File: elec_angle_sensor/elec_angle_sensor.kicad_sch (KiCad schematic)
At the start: 13 parts, among them J7 JST SH, U1 AS5600L

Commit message: [update] Full schematic + positionning
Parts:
- added H4: Mounting Holes M2,5, MountingHole:MountingHole_2.7mm_M2.5_ISO7380_Pad_TopBottom, symbol Mechanical:MountingHole_Pad
- added H5: MountingHole_Pad, MountingHole:MountingHole_2.7mm_M2.5_ISO7380_Pad_TopBottom, symbol Mechanical:MountingHole_Pad
- added H6, H7: Centering Hole 2 mm, Library_Pollen:MountingHole_2.0mm, symbol Mechanical:MountingHole
- added J1: JST SH, Connector_JST:JST_SH_SM04B-SRSS-TB_1x04-1MP_P1.00mm_Horizontal, symbol Connector_Generic_MountingPin:Conn_01x04_MountingPin
- G1: footprint Sparkfun-Qwiic:qwiic_5mm -> Library_Pollen:Logo_qwiic_5mm; symbol Sparkfun-Qwiic:qwiic_Logo -> Library_Pollen:Logo qwiic; now in the parts list
- J7: footprint Connector_JST:JST_SH_BM04B-SRSS-TB_1x04-1MP_P1.00mm_Vertical -> Connector_JST:JST_SH_SM04B-SRSS-TB_1x04-1MP_P1.00mm_Horizontal; LCSC Part C160390 -> C160404
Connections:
- net +3V3: now also J1.2 (Pin_2)
- net GND: now also H4.1, H5.1, J1.1 (Pin_1), J1.MP (MountPin)
- net at D1.3 (K), J7.3 (Pin_3), R1.2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: now also J1.3 (Pin_3)
- net at D1.4 (K), J7.4 (Pin_4), R2.2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: now also J1.4 (Pin_4)
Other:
- moved on the sheet: J7

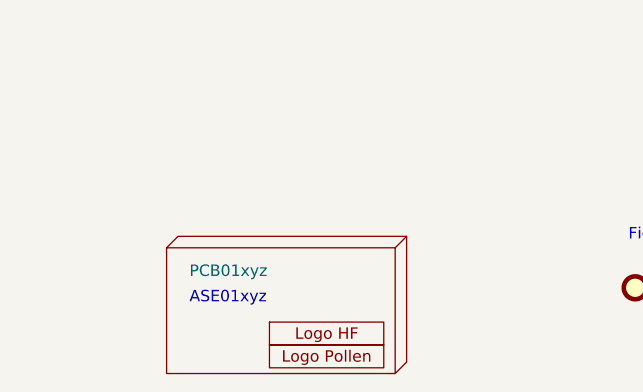
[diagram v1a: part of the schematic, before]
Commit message: [update] Angle+IMU are routed ERC OK
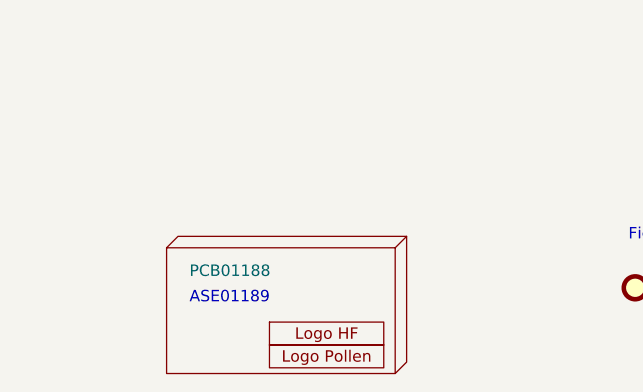
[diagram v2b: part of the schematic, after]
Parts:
- H1: value PCB01xyz -> PCB01188
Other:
- note added: "ASE01189"
- note removed: "ASE01xyz"
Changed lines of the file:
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@@
 		)
 	)
-	(text "ASE01xyz"
+	(text "ASE01189"
 		(exclude_from_sim no)
 		(at 38.1 172.085 0)
@@
 			)
 		)
-		(property "Value" "PCB01xyz"
+		(property "Value" "PCB01188"
 			(at 38.1 168.275 0)
 			(effects

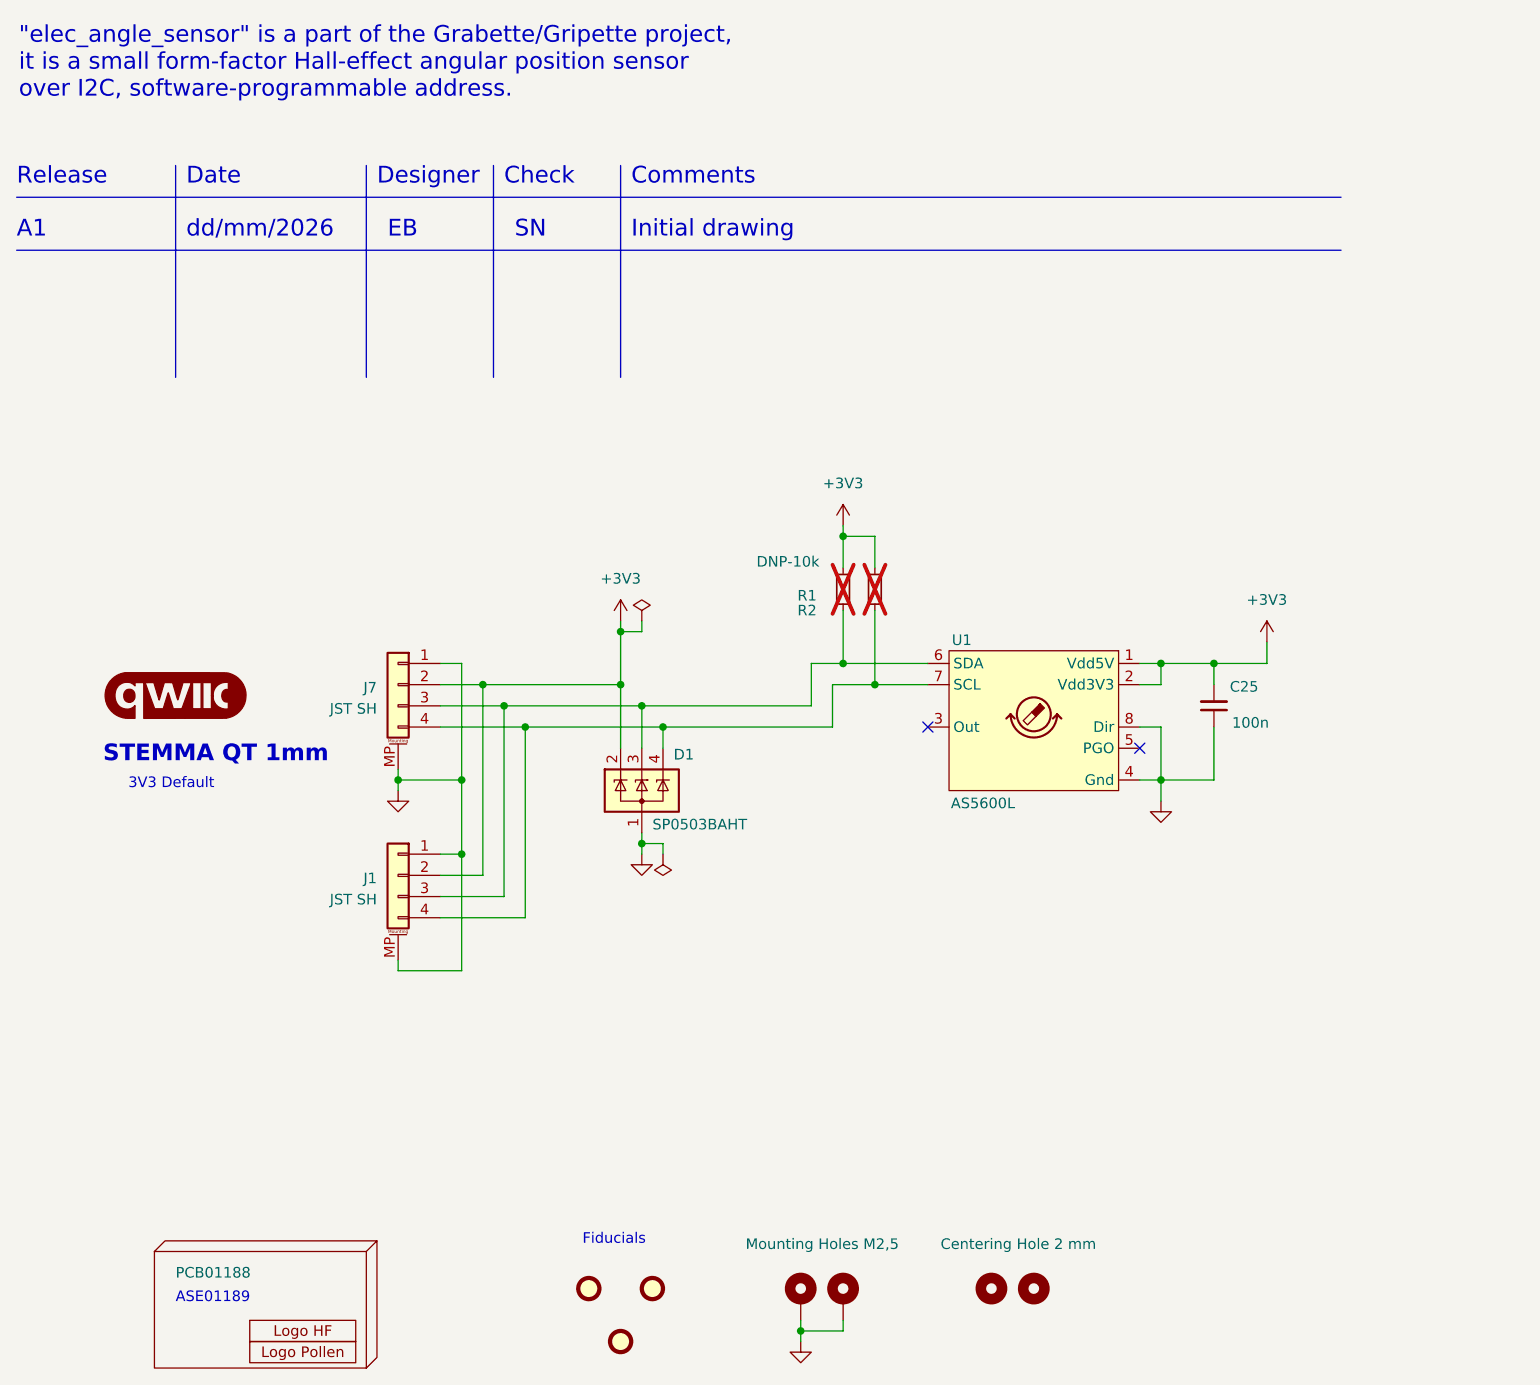
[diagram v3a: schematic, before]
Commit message: [added] Gripette-specific DCDC
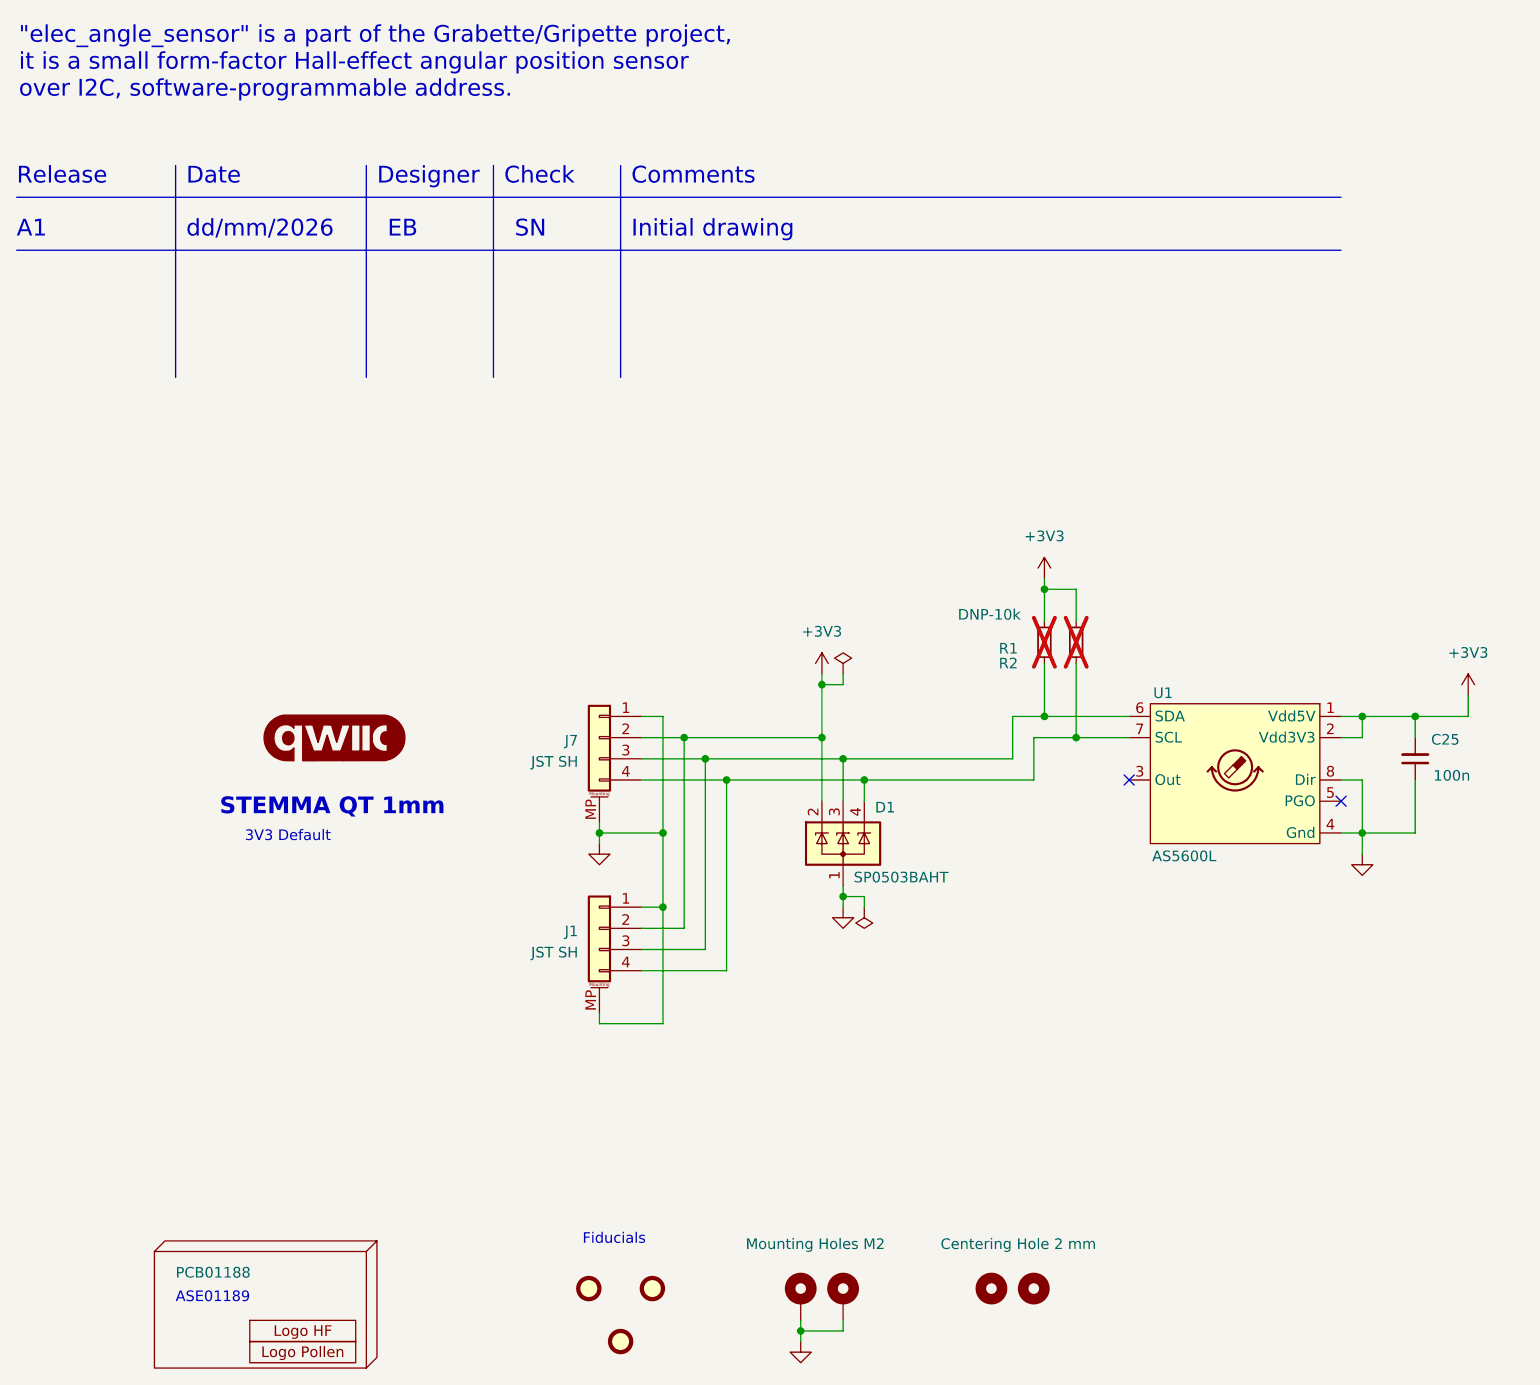
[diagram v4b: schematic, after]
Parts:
- H4: value Mounting Holes M2,5 -> Mounting Holes M2; footprint MountingHole:MountingHole_2.7mm_M2.5_ISO7380_Pad_TopBottom -> MountingHole:MountingHole_2.2mm_M2_ISO7380_Pad_TopBottom
- H5: value MountingHole_Pad -> Mounting Holes M2; footprint MountingHole:MountingHole_2.7mm_M2.5_ISO7380_Pad_TopBottom -> MountingHole:MountingHole_2.2mm_M2_ISO7380_Pad_TopBottom
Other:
- moved on the sheet: C25, D1, J1, J7, R1, R2, U1

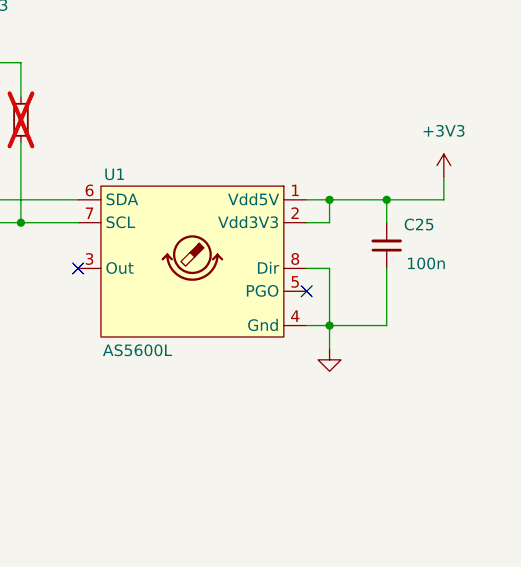
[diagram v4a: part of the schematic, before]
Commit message: [added] BMS/Charger
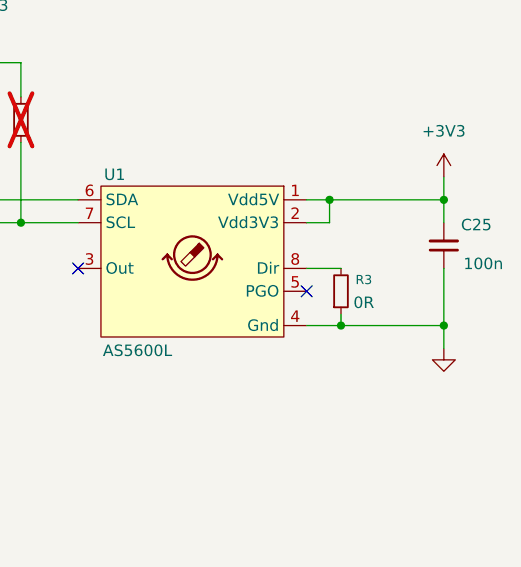
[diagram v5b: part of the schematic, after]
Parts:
- added R3: 0R, Resistor_SMD:R_0402_1005Metric, symbol Device:R_Small
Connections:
- net GND: now also R3.1; no longer U1.8 (Dir)
- new net: R3.2, U1.8 (Dir)
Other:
- moved on the sheet: C25
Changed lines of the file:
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@@
 	)
 	(junction
+		(at 193.04 115.57)
+		(diameter 0)
+		(color 0 0 0 0)
+	)
+	(junction
 		(at 96.52 124.46)
 		(diameter 0)
@@
 	)
 	(junction
-		(at 104.14 109.22)
+		(at 181.61 115.57)
 		(diameter 0)
 		(color 0 0 0 0)
 	)
 	(junction
-		(at 186.69 101.6)
+		(at 104.14 109.22)
 		(diameter 0)
 		(color 0 0 0 0)
@@
 	)
 	(junction
-		(at 180.34 115.57)
+		(at 193.04 101.6)
 		(diameter 0)
 		(color 0 0 0 0)
@@
 	(wire
 		(pts
-			(xy 186.69 115.57) (xy 180.34 115.57)
-		)
-		(stroke
-			(width 0)
-			(type default)
-		)
-	)
-	(wire
-		(pts
 			(xy 88.9 115.57) (xy 88.9 116.84)
 		)
@@
 	(wire
 		(pts
-			(xy 180.34 115.57) (xy 180.34 118.11)
+			(xy 193.04 115.57) (xy 193.04 118.11)
 		)
 		(stroke
@@
 	(wire
 		(pts
-			(xy 177.8 115.57) (xy 180.34 115.57)
+			(xy 177.8 115.57) (xy 181.61 115.57)
 		)
 		(stroke
@@
 	(wire
 		(pts
-			(xy 180.34 109.22) (xy 180.34 115.57)
+			(xy 181.61 114.3) (xy 181.61 115.57)
 		)
 		(stroke
@@
 	(wire
 		(pts
-			(xy 186.69 101.6) (xy 193.04 101.6)
+			(xy 120.65 109.22) (xy 104.14 109.22)
 		)
 		(stroke
@@
 	(wire
 		(pts
-			(xy 120.65 109.22) (xy 104.14 109.22)
+			(xy 115.57 97.79) (xy 115.57 96.52)
 		)
 		(stroke
@@
 	(wire
 		(pts
-			(xy 115.57 97.79) (xy 115.57 96.52)
+			(xy 120.65 109.22) (xy 120.65 111.76)
 		)
 		(stroke
@@
 	(wire
 		(pts
-			(xy 120.65 109.22) (xy 120.65 111.76)
+			(xy 177.8 109.22) (xy 181.61 109.22)
 		)
 		(stroke
@@
 	(wire
 		(pts
-			(xy 177.8 109.22) (xy 180.34 109.22)
+			(xy 93.98 132.08) (xy 104.14 132.08)
 		)
 		(stroke
@@
 	(wire
 		(pts
-			(xy 93.98 132.08) (xy 104.14 132.08)
+			(xy 193.04 101.6) (xy 193.04 104.14)
 		)
 		(stroke
@@
 	(wire
 		(pts
-			(xy 186.69 101.6) (xy 186.69 104.14)
+			(xy 152.4 104.14) (xy 146.05 104.14)
 		)
 		(stroke
@@
 	(wire
 		(pts
-			(xy 152.4 104.14) (xy 146.05 104.14)
+			(xy 118.11 96.52) (xy 118.11 97.79)
 		)
 		(stroke
@@
 	(wire
 		(pts
-			(xy 118.11 96.52) (xy 118.11 97.79)
+			(xy 181.61 115.57) (xy 193.04 115.57)
 		)
 		(stroke
@@
 	(wire
 		(pts
-			(xy 186.69 109.22) (xy 186.69 115.57)
+			(xy 193.04 109.22) (xy 193.04 115.57)
 		)
 		(stroke
@@
 	(wire
 		(pts
-			(xy 186.69 101.6) (xy 180.34 101.6)
+			(xy 180.34 101.6) (xy 193.04 101.6)
 		)
 		(stroke
@@
 		)
 		(instances
-			(project "elec_forcathon"
+			(project "elec_angle_sensor"
 				(path "/bc05f5da-608c-4912-90e4-36b13d989976"
 					(reference "H1")
@@
 		)
 		(instances
-			(project "elec_forcathon"
+			(project "elec_angle_sensor"
 				(path "/bc05f5da-608c-4912-90e4-36b13d989976"
 					(reference "FID3")
@@
 		)
 		(instances
-			(project ""
+			(project "elec_angle_sensor"
 				(path "/bc05f5da-608c-4912-90e4-36b13d989976"
 					(reference "U1")
@@
 	(symbol
 		(lib_id "power:GND")
-		(at 180.34 118.11 0)
+		(at 193.04 118.11 0)
 		(mirror y)
 		(unit 1)
@@
 		(fields_autoplaced yes)
 		(property "Reference" "#PWR01"
-			(at 180.34 124.46 0)
+			(at 193.04 124.46 0)
 			(effects
 				(font
@@
 		)
 		(property "Value" "GND"
-			(at 180.34 123.19 0)
+			(at 193.04 123.19 0)
 			(effects
 				(font
@@
 		)
 		(property "Footprint" ""
-			(at 180.34 118.11 0)
+			(at 193.04 118.11 0)
 			(effects
 				(font
@@
 		)
 		(property "Datasheet" ""
-			(at 180.34 118.11 0)
+			(at 193.04 118.11 0)
 			(effects
 				(font
@@
 		)
 		(property "Description" "Power symbol creates a global label with name \"GND\" , ground"
-			(at 180.34 118.11 0)
+			(at 193.04 118.11 0)
 			(effects
 				(font
@@
 		)
 		(instances
-			(project ""
+			(project "elec_angle_sensor"
 				(path "/bc05f5da-608c-4912-90e4-36b13d989976"
 					(reference "#PWR01")
@@
 	)
 	(symbol
+		(lib_id "Device:R_Small")
+		(at 181.61 111.76 0)
+		(mirror x)
+		(unit 1)
+		(exclude_from_sim no)
+		(in_bom yes)
+		(on_board yes)
+		(dnp no)
+		(property "Reference" "R3"
+			(at 184.15 110.49 0)
+			(effects
+				(font
+					(size 1.016 1.016)
+				)
+			)
+		)
+		(property "Value" "0R"
+			(at 184.15 113.03 0)
+			(effects
+				(font
+					(size 1.27 1.27)
+				)
+			)
+		)
+		(property "Footprint" "Resistor_SMD:R_0402_1005Metric"
+			(at 181.61 111.76 0)
+			(effects
+				(font
+					(size 1.27 1.27)
+				)
+				(hide yes)
+			)
+		)
+		(property "Datasheet" "~"
+			(at 181.61 111.76 0)
+			(effects
+				(font
+					(size 1.27 1.27)
+				)
+				(hide yes)
+			)
+		)
+		(property "Description" "Resistor, small symbol"
+			(at 181.61 111.76 0)
+			(effects
+				(font
+					(size 1.27 1.27)
+				)
+				(hide yes)
+			)
+		)
+		(property "LCSC Part" "C17168"
+			(at 181.61 111.76 90)
+			(effects
+				(font
+					(size 1.27 1.27)
+				)
+				(hide yes)
+			)
+		)
+		(pin "2"
+		)
+		(pin "1"
+		)
+		(instances
+			(project "elec_angle_sensor"
+				(path "/bc05f5da-608c-4912-90e4-36b13d989976"
+					(reference "R3")
+					(unit 1)
+				)
+			)
+		)
+	)
+	(symbol
 		(lib_id "power:GND")
 		(at 113.03 176.53 0)
@@
 		)
 		(instances
-			(project "elec_forcathon"
+			(project "elec_angle_sensor"
 				(path "/bc05f5da-608c-4912-90e4-36b13d989976"
 					(reference "FID1")
@@
 		)
 		(instances
-			(project ""
+			(project "elec_angle_sensor"
 				(path "/bc05f5da-608c-4912-90e4-36b13d989976"
 					(reference "#FLG01")
@@
 		)
 		(instances
-			(project ""
+			(project "elec_angle_sensor"
 				(path "/bc05f5da-608c-4912-90e4-36b13d989976"
 					(reference "#PWR03")
@@
 		)
 		(instances
-			(project "elec_forcathon"
+			(project "elec_angle_sensor"
 				(path "/bc05f5da-608c-4912-90e4-36b13d989976"
 					(reference "FID2")
@@
 	(symbol
 		(lib_id "Device:C_Small")
-		(at 186.69 106.68 0)
+		(at 193.04 106.68 0)
 		(mirror x)
 		(unit 1)
@@
 		(dnp no)
 		(property "Reference" "C25"
-			(at 192.024 104.394 0)
+			(at 198.374 104.394 0)
 			(effects
 				(font
@@
 		)
 		(property "Value" "100n"
-			(at 193.294 108.712 0)
+			(at 199.644 108.712 0)
 			(effects
 				(font
@@
 		)
 		(property "Footprint" "Capacitor_SMD:C_0402_1005Metric"
-			(at 186.69 106.68 0)
+			(at 193.04 106.68 0)
 			(effects
 				(font
@@
 		)
 		(property "Datasheet" "~"
-			(at 186.69 106.68 0)
+			(at 193.04 106.68 0)
 			(effects
 				(font
@@
 		)
 		(property "Description" "Unpolarized capacitor, small symbol"
-			(at 186.69 106.68 0)
+			(at 193.04 106.68 0)
 			(effects
 				(font
@@
 		)
 		(property "Man." ""
-			(at 186.69 106.68 0)
+			(at 193.04 106.68 0)
 			(effects
 				(font
@@
 		)
 		(property "Man. Ref." ""
-			(at 186.69 106.68 0)
+			(at 193.04 106.68 0)
 			(effects
 				(font
@@
 		)
 		(property "LCSC Part" "C307331"
-			(at 186.69 106.68 0)
+			(at 193.04 106.68 0)
 			(effects
 				(font
@@
 		)
 		(instances
-			(project ""
+			(project "elec_angle_sensor"
 				(path "/bc05f5da-608c-4912-90e4-36b13d989976"
 					(reference "H6")
@@
 		)
 		(instances
-			(project "elec_forcathon"
+			(project "elec_angle_sensor"
 				(path "/bc05f5da-608c-4912-90e4-36b13d989976"
 					(reference "H3")
@@
 		)
 		(instances
-			(project ""
+			(project "elec_angle_sensor"
 				(path "/bc05f5da-608c-4912-90e4-36b13d989976"
 					(reference "H2")

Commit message: [update] Added error to gripette, going to B1
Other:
- note added: "Can be software-changed (+OTP)"
- note added: "Default I2C add. 0x40"
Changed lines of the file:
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@@
+		)
+	)
+	(text "Can be software-changed (+OTP)"
+		(exclude_from_sim no)
+		(at 166.878 131.318 0)
+		(effects
+			(font
+				(size 1.27 1.27)
+			)
 		)
 	)
@@
 		)
 	)
+	(text "Default I2C add. 0x40"
+		(exclude_from_sim no)
+		(at 166.624 128.016 0)
+		(effects
+			(font
+				(size 2 2)
+				(thickness 0.4)
+				(bold yes)
+			)
+		)
+	)
